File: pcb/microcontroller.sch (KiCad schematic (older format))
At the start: 0 parts

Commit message: Add STM32F072CBT6 library and microcontroller sheet
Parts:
- added C? (x3): 0.1uF, symbol C
- added C?: 10nF, symbol C
- added U?: STM32F072CBT6, symbol STM32F072CBT6
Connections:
- net labels added: +BATT, GND, GNDA, USB_D+, USB_D-, VAA, VDD
- wire segments 0 -> 27
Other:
- note added: "NOTE: Place near VDDA (9)"
- note added: "NOTE: Place one near each\nVDD pin (24, 48) and one\nnear VDDIO2 (36)"
- note added: "NOTE: VDD supply needs 4.7uF across it\nVAA supply needs 1uF across it"
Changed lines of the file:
@@
 LIBS:uSD_holder
 LIBS:radiometrix_mtx2
+LIBS:stm32f072cbt6
 LIBS:woodchuck-cache
 EELAYER 25 0
@@
 $Descr A4 11693 8268
 encoding utf-8
-Sheet 1 6
+Sheet 4 6
 Title ""
 Date ""
@@
 Comment4 ""
 $EndDescr
+$Comp
+L STM32F072CBT6 U?
+U 1 1 565B237E
+P 5050 2800
+F 0 "U?" H 5100 2850 60  0000 C CNN
+F 1 "STM32F072CBT6" H 6300 2850 60  0000 C CNN
+F 2 "" H 5400 2900 60  0000 C CNN
+F 3 "" H 5400 2900 60  0000 C CNN
+	1    5050 2800
+	1    0    0    -1
+$EndComp
+$Comp
+L GND #PWR01
+U 1 1 565B23CF
+P 5600 5600
+F 0 "#PWR01" H 5600 5350 50  0001 C CNN
+F 1 "GND" H 5600 5450 50  0000 C CNN
+F 2 "" H 5600 5600 60  0000 C CNN
+F 3 "" H 5600 5600 60  0000 C CNN
+	1    5600 5600
+	1    0    0    -1
+$EndComp
+$Comp
+L GNDA #PWR02
+U 1 1 565B2430
+P 5800 5600
+F 0 "#PWR02" H 5800 5350 50  0001 C CNN
+F 1 "GNDA" H 5800 5450 50  0000 C CNN
+F 2 "" H 5800 5600 60  0000 C CNN
+F 3 "" H 5800 5600 60  0000 C CNN
+	1    5800 5600
+	1    0    0    -1
+$EndComp
+Wire Wire Line
+	5500 5400 5500 5500
+Wire Wire Line
+	5500 5500 5700 5500
+Wire Wire Line
+	5600 5400 5600 5600
+Connection ~ 5600 5500
+Wire Wire Line
+	5700 5500 5700 5400
+Wire Wire Line
+	5800 5400 5800 5600
+$Comp
+L C C?
+U 1 1 565B2484
+P 4300 2300
+F 0 "C?" H 4325 2400 50  0000 L CNN
+F 1 "0.1uF" H 4325 2200 50  0000 L CNN
+F 2 "" H 4338 2150 30  0000 C CNN
+F 3 "" H 4300 2300 60  0000 C CNN
+	1    4300 2300
+	1    0    0    -1
+$EndComp
+$Comp
+L VDD #PWR03
+U 1 1 565B24B5
+P 5600 2400
+F 0 "#PWR03" H 5600 2250 50  0001 C CNN
+F 1 "VDD" H 5600 2550 50  0000 C CNN
+F 2 "" H 5600 2400 60  0000 C CNN
+F 3 "" H 5600 2400 60  0000 C CNN
+	1    5600 2400
+	1    0    0    -1
+$EndComp
+$Comp
+L VAA #PWR04
+U 1 1 565B24CD
+P 5800 2400
+F 0 "#PWR04" H 5800 2250 50  0001 C CNN
+F 1 "VAA" H 5800 2550 50  0000 C CNN
+F 2 "" H 5800 2400 60  0000 C CNN
+F 3 "" H 5800 2400 60  0000 C CNN
+	1    5800 2400
+	1    0    0    -1
+$EndComp
+$Comp
+L VDD #PWR05
+U 1 1 565B24E5
+P 6000 2400
+F 0 "#PWR05" H 6000 2250 50  0001 C CNN
+F 1 "VDD" H 6000 2550 50  0000 C CNN
+F 2 "" H 6000 2400 60  0000 C CNN
+F 3 "" H 6000 2400 60  0000 C CNN
+	1    6000 2400
+	1    0    0    -1
+$EndComp
+Wire Wire Line
+	5800 2600 5800 2400
+Wire Wire Line
+	5700 2600 5700 2500
+Wire Wire Line
+	5700 2500 5600 2500
+Wire Wire Line
+	5600 2400 5600 2600
+Connection ~ 5600 2500
+$Comp
+L +BATT #PWR06
+U 1 1 565B2BDD
+P 5400 2400
+F 0 "#PWR06" H 5400 2250 50  0001 C CNN
+F 1 "+BATT" H 5400 2540 50  0000 C CNN
+F 2 "" H 5400 2400 60  0000 C CNN
+F 3 "" H 5400 2400 60  0000 C CNN
+	1    5400 2400
+	1    0    0    -1
+$EndComp
+Wire Wire Line
+	5500 2600 5500 2500
+Wire Wire Line
+	5500 2500 5400 2500
+Wire Wire Line
+	5400 2500 5400 2400
+$Comp
+L VDD #PWR07
+U 1 1 565B2C77
+P 4300 1950
+F 0 "#PWR07" H 4300 1800 50  0001 C CNN
+F 1 "VDD" H 4300 2100 50  0000 C CNN
+F 2 "" H 4300 1950 60  0000 C CNN
+F 3 "" H 4300 1950 60  0000 C CNN
+	1    4300 1950
+	1    0    0    -1
+$EndComp
+Wire Wire Line
+	4300 1950 4300 2150
+$Comp
+L GND #PWR09
+U 1 1 565B2D06
+P 4300 2650
+F 0 "#PWR09" H 4300 2400 50  0001 C CNN
+F 1 "GND" H 4300 2500 50  0000 C CNN
+F 2 "" H 4300 2650 60  0000 C CNN
+F 3 "" H 4300 2650 60  0000 C CNN
+	1    4300 2650
+	1    0    0    -1
+$EndComp
+Wire Wire Line
+	4300 2450 4300 2650
+$Comp
+L C C?
+U 1 1 565B2D3B
+P 4050 2300
+F 0 "C?" H 4075 2400 50  0000 L CNN
+F 1 "0.1uF" H 4075 2200 50  0000 L CNN
+F 2 "" H 4088 2150 30  0000 C CNN
+F 3 "" H 4050 2300 60  0000 C CNN
+	1    4050 2300
+	1    0    0    -1
+$EndComp
+Connection ~ 4300 2550
+Wire Wire Line
+	4050 2450 4050 2550
+Wire Wire Line
+	4050 2150 4050 2050
+Connection ~ 4300 2050
+Text Notes 3900 2800 1    60   ~ 0
+NOTE: Place one near each\nVDD pin (24, 48) and one\nnear VDDIO2 (36)
+Wire Wire Line
+	4050 2550 4550 2550
+Wire Wire Line
+	4050 2050 4550 2050
+$Comp
+L C C?
+U 1 1 565B339D
+P 2950 2300
+F 0 "C?" H 2975 2400 50  0000 L CNN
+F 1 "10nF" H 2975 2200 50  0000 L CNN
+F 2 "" H 2988 2150 30  0000 C CNN
+F 3 "" H 2950 2300 60  0000 C CNN
+	1    2950 2300
+	1    0    0    -1
+$EndComp
+$Comp
+L VDD #PWR?
+U 1 1 565B33A3
+P 2950 2050
+F 0 "#PWR?" H 2950 1900 50  0001 C CNN
+F 1 "VDD" H 2950 2200 50  0000 C CNN
+F 2 "" H 2950 2050 60  0000 C CNN
+F 3 "" H 2950 2050 60  0000 C CNN
+	1    2950 2050
+	1    0    0    -1
+$EndComp
+Wire Wire Line
+	2950 2050 2950 2150
+$Comp
+L GND #PWR?
+U 1 1 565B33AB
+P 2950 2550
+F 0 "#PWR?" H 2950 2300 50  0001 C CNN
+F 1 "GND" H 2950 2400 50  0000 C CNN
+F 2 "" H 2950 2550 60  0000 C CNN
+F 3 "" H 2950 2550 60  0000 C CNN
+	1    2950 2550
+	1    0    0    -1
+$EndComp
+Wire Wire Line
+	2950 2450 2950 2650
+Text Notes 2750 2800 1    60   ~ 0
+NOTE: Place near VDDA (9)
+$Comp
+L C C?
+U 1 1 565B3429
+P 4550 2300
+F 0 "C?" H 4575 2400 50  0000 L CNN
+F 1 "0.1uF" H 4575 2200 50  0000 L CNN
+F 2 "" H 4588 2150 30  0000 C CNN
+F 3 "" H 4550 2300 60  0000 C CNN
+	1    4550 2300
+	1    0    0    -1
+$EndComp
+Wire Wire Line
+	4550 2050 4550 2150
+Wire Wire Line
+	4550 2550 4550 2450
+Wire Wire Line
+	5900 2600 5900 2500
+Wire Wire Line
+	5900 2500 6000 2500
+Wire Wire Line
+	6000 2500 6000 2400
+Wire Wire Line
+	4850 4700 4400 4700
+Wire Wire Line
+	4850 4800 4400 4800
+Text GLabel 4400 4700 0    60   Input ~ 0
+USB_D-
+Text GLabel 4400 4800 0    60   Input ~ 0
+USB_D+
+Text Notes 6250 2500 0    60   ~ 0
+NOTE: VDD supply needs 4.7uF across it\nVAA supply needs 1uF across it
 $EndSCHEMATC

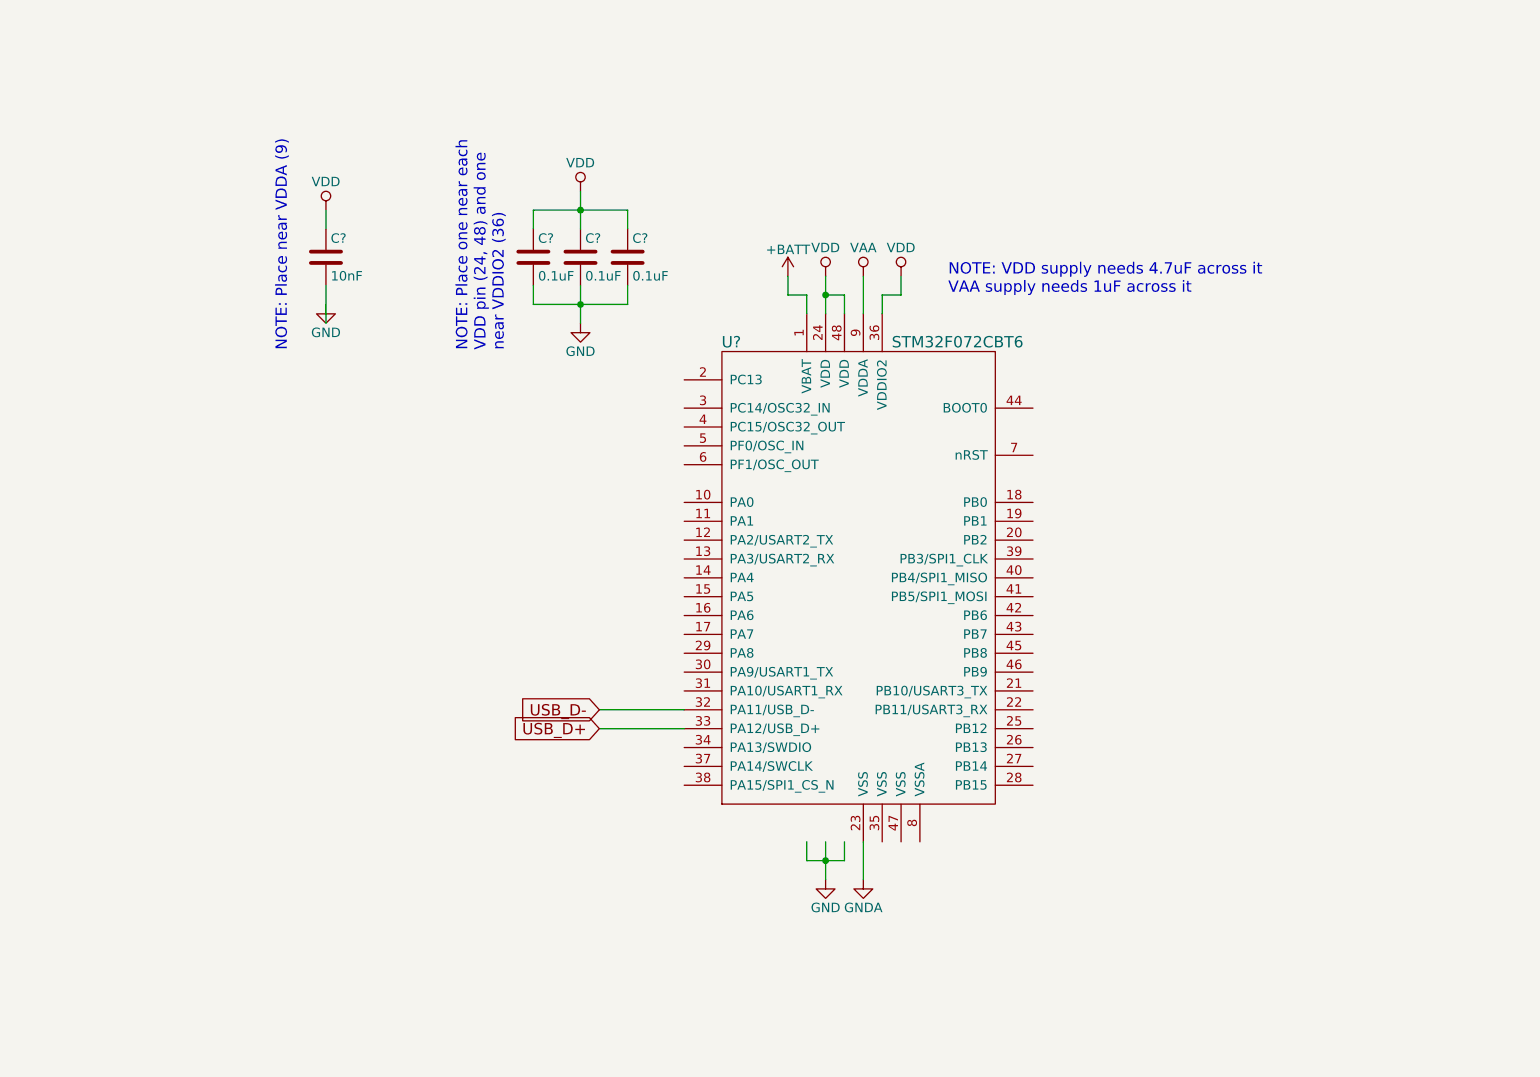
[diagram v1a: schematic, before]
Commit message: Add SWD port to microcontroller sheet
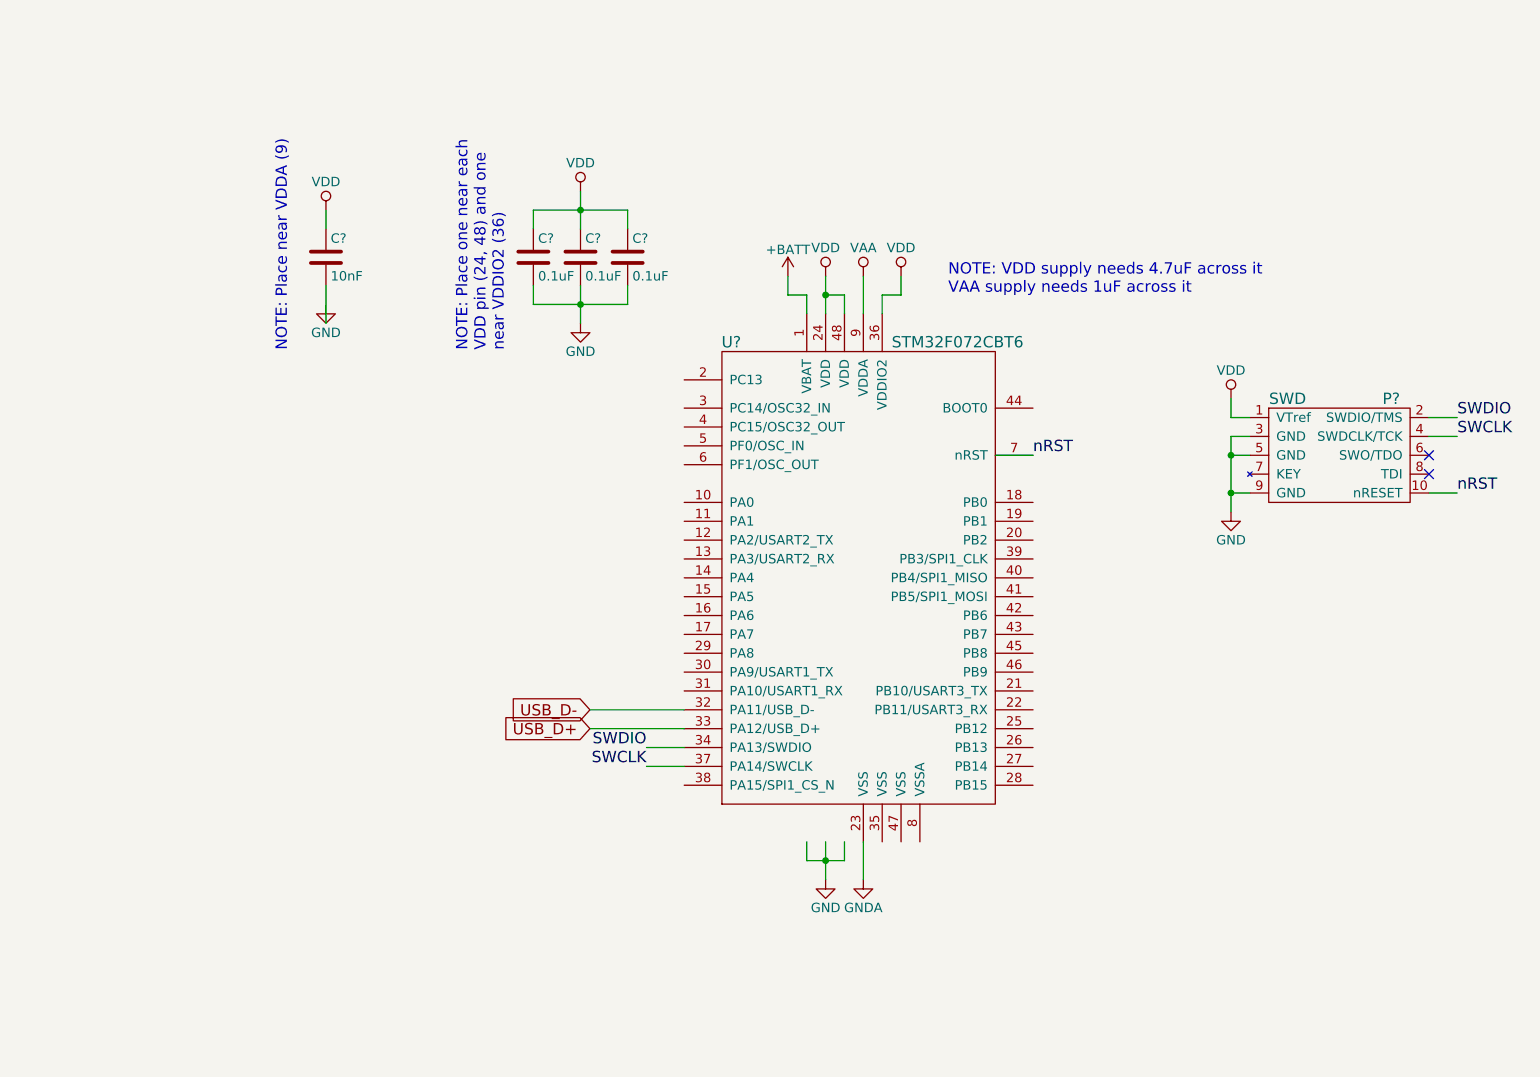
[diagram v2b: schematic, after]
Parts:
- added P?: SWD, symbol SWD
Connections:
- net labels added: SWCLK, SWDIO, nRST
- wire segments 27 -> 48
- no-connect marks 0 -> 2
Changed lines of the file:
@@
 	5500 5400 5500 5500
 Wire Wire Line
-	5500 5500 5700 5500
-Wire Wire Line
-	5600 5400 5600 5600
+	5500 5500 5600 5500
+Wire Wire Line
+	5600 5500 5700 5500
+Wire Wire Line
+	5600 5400 5600 5500
+Wire Wire Line
+	5600 5500 5600 5600
 Connection ~ 5600 5500
 Wire Wire Line
@@
 	5700 2500 5600 2500
 Wire Wire Line
-	5600 2400 5600 2600
+	5600 2400 5600 2500
+Wire Wire Line
+	5600 2500 5600 2600
 Connection ~ 5600 2500
 $Comp
@@
 $EndComp
 Wire Wire Line
-	4300 1950 4300 2150
-$Comp
-L GND #PWR09
+	4300 1950 4300 2050
+Wire Wire Line
+	4300 2050 4300 2150
+$Comp
+L GND #PWR08
 U 1 1 565B2D06
 P 4300 2650
-F 0 "#PWR09" H 4300 2400 50  0001 C CNN
+F 0 "#PWR08" H 4300 2400 50  0001 C CNN
 F 1 "GND" H 4300 2500 50  0000 C CNN
 F 2 "" H 4300 2650 60  0000 C CNN
@@
 $EndComp
 Wire Wire Line
-	4300 2450 4300 2650
+	4300 2450 4300 2550
+Wire Wire Line
+	4300 2550 4300 2650
 $Comp
 L C C?
@@
 NOTE: Place one near each\nVDD pin (24, 48) and one\nnear VDDIO2 (36)
 Wire Wire Line
-	4050 2550 4550 2550
-Wire Wire Line
-	4050 2050 4550 2050
+	4050 2550 4300 2550
+Wire Wire Line
+	4300 2550 4550 2550
+Wire Wire Line
+	4050 2050 4300 2050
+Wire Wire Line
+	4300 2050 4550 2050
 $Comp
 L C C?
@@
 $EndComp
 $Comp
-L VDD #PWR?
+L VDD #PWR09
 U 1 1 565B33A3
 P 2950 2050
-F 0 "#PWR?" H 2950 1900 50  0001 C CNN
+F 0 "#PWR09" H 2950 1900 50  0001 C CNN
 F 1 "VDD" H 2950 2200 50  0000 C CNN
 F 2 "" H 2950 2050 60  0000 C CNN
@@
 	2950 2050 2950 2150
 $Comp
-L GND #PWR?
+L GND #PWR010
 U 1 1 565B33AB
 P 2950 2550
-F 0 "#PWR?" H 2950 2300 50  0001 C CNN
+F 0 "#PWR010" H 2950 2300 50  0001 C CNN
 F 1 "GND" H 2950 2400 50  0000 C CNN
 F 2 "" H 2950 2550 60  0000 C CNN
@@
 	6000 2500 6000 2400
 Wire Wire Line
-	4850 4700 4400 4700
-Wire Wire Line
-	4850 4800 4400 4800
-Text GLabel 4400 4700 0    60   Input ~ 0
+	4850 4700 4350 4700
+Wire Wire Line
+	4850 4800 4350 4800
+Text GLabel 4350 4700 0    60   Input ~ 0
 USB_D-
-Text GLabel 4400 4800 0    60   Input ~ 0
+Text GLabel 4350 4800 0    60   Input ~ 0
 USB_D+
 Text Notes 6250 2500 0    60   ~ 0
 NOTE: VDD supply needs 4.7uF across it\nVAA supply needs 1uF across it
+$Comp
+L SWD P?
+U 1 1 565B3F04
+P 8350 3350
+F 0 "P?" H 8600 3650 60  0000 C CNN
+F 1 "SWD" H 8050 3650 60  0000 C CNN
+F 2 "" H 8700 3150 60  0000 C CNN
+F 3 "" H 8700 3150 60  0000 C CNN
+	1    8350 3350
+	1    0    0    -1
+$EndComp
+Wire Wire Line
+	6500 3350 6700 3350
+Text Label 6700 3350 0    60   ~ 0
+nRST
+Wire Wire Line
+	8800 3550 8950 3550
+Text Label 8950 3550 0    60   ~ 0
+nRST
+Wire Wire Line
+	8800 3250 8950 3250
+Wire Wire Line
+	8800 3150 8950 3150
+NoConn ~ 8800 3350
+NoConn ~ 8800 3450
+Text Label 8950 3250 0    60   ~ 0
+SWCLK
+Text Label 8950 3150 0    60   ~ 0
+SWDIO
+Wire Wire Line
+	4850 4900 4650 4900
+Wire Wire Line
+	4850 5000 4650 5000
+Text Label 4650 4900 2    60   ~ 0
+SWDIO
+Text Label 4650 5000 2    60   ~ 0
+SWCLK
+$Comp
+L VDD #PWR?
+U 1 1 565B450F
+P 7750 3050
+F 0 "#PWR?" H 7750 2900 50  0001 C CNN
+F 1 "VDD" H 7750 3200 50  0000 C CNN
+F 2 "" H 7750 3050 60  0000 C CNN
+F 3 "" H 7750 3050 60  0000 C CNN
+	1    7750 3050
+	1    0    0    -1
+$EndComp
+Wire Wire Line
+	7850 3150 7750 3150
+Wire Wire Line
+	7750 3150 7750 3050
+$Comp
+L GND #PWR?
+U 1 1 565B4620
+P 7750 3650
+F 0 "#PWR?" H 7750 3400 50  0001 C CNN
+F 1 "GND" H 7750 3500 50  0000 C CNN
+F 2 "" H 7750 3650 60  0000 C CNN
+F 3 "" H 7750 3650 60  0000 C CNN
+	1    7750 3650
+	1    0    0    -1
+$EndComp
+Wire Wire Line
+	7850 3550 7750 3550
+Wire Wire Line
+	7750 3250 7750 3350
+Wire Wire Line
+	7750 3350 7750 3550
+Wire Wire Line
+	7750 3550 7750 3650
+Wire Wire Line
+	7850 3350 7750 3350
+Connection ~ 7750 3550
+Wire Wire Line
+	7850 3250 7750 3250
+Connection ~ 7750 3350
 $EndSCHEMATC

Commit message: Add JSTA-4 connector
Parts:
- added J?: JSTA-4, symbol JSTA-4
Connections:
- net labels added: EXT_RX, EXT_TX
- wire segments 48 -> 56
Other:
- note added: "EXT PORT"
- note added: "SUPPLY CAPS"
- note added: "SWD PORT"
- moved on the sheet: C?, P?
